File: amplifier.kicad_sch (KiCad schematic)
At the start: 16 parts, among them U5 PAM8403D

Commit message: Added more connections
Updated footprints for pin heads and speakers
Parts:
- removed C13: 470u, Capacitor_SMD:CP_Elec_8x10.5, symbol Device:C
- added C13: 470u, Capacitor_SMD:CP_Elec_8x10.5, symbol Device:C_Polarized
- LS1, LS2: footprint (none) -> Connector_PinHeader_2.00mm:PinHeader_1x02_P2.00mm_Vertical_SMD_Pin1Left
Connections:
- net 3.3V_IN: now also C13.1
- net GND: now also C13.2
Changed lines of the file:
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@@
 	(symbol
 		(lib_id "Device:C")
+		(at 95.25 63.5 0)
+		(unit 1)
+		(exclude_from_sim no)
+		(in_bom yes)
+		(on_board yes)
+		(dnp no)
+		(property "Reference" "C14"
+			(at 88.9 61.976 0)
+			(effects
+				(font
+					(size 1.27 1.27)
+				)
+				(justify left)
+			)
+		)
+		(property "Value" "1u"
+			(at 88.9 64.516 0)
+			(effects
+				(font
+					(size 1.27 1.27)
+				)
+				(justify left)
+			)
+		)
+		(property "Footprint" "Capacitor_SMD:C_0603_1608Metric"
+			(at 96.2152 67.31 0)
+			(effects
+				(font
+					(size 1.27 1.27)
+				)
+				(hide yes)
+			)
+		)
+		(property "Datasheet" "~"
+			(at 95.25 63.5 0)
+			(effects
+				(font
+					(size 1.27 1.27)
+				)
+				(hide yes)
+			)
+		)
+		(property "Description" "Unpolarized capacitor"
+			(at 95.25 63.5 0)
+			(effects
+				(font
+					(size 1.27 1.27)
+				)
+				(hide yes)
+			)
+		)
+		(pin "1"
+		)
+		(pin "2"
+		)
+		(instances
+			(project "plant caretaker"
+				(path "/23b35dcc-615e-4aec-abee-c26cc3d8b906/64bd70cc-1431-45fc-8946-041e9631b1bb"
+					(reference "C14")
+					(unit 1)
+				)
+			)
+		)
+	)
+	(symbol
+		(lib_id "power:GND")
+		(at 165.1 69.85 0)
+		(unit 1)
+		(exclude_from_sim no)
+		(in_bom yes)
+		(on_board yes)
+		(dnp no)
+		(fields_autoplaced yes)
+		(property "Reference" "#PWR033"
+			(at 165.1 76.2 0)
+			(effects
+				(font
+					(size 1.27 1.27)
+				)
+				(hide yes)
+			)
+		)
+		(property "Value" "GND"
+			(at 165.1 74.93 0)
+			(effects
+				(font
+					(size 1.27 1.27)
+				)
+			)
+		)
+		(property "Footprint" ""
+			(at 165.1 69.85 0)
+			(effects
+				(font
+					(size 1.27 1.27)
+				)
+				(hide yes)
+			)
+		)
+		(property "Datasheet" ""
+			(at 165.1 69.85 0)
+			(effects
+				(font
+					(size 1.27 1.27)
+				)
+				(hide yes)
+			)
+		)
+		(property "Description" "Power symbol creates a global label with name \"GND\" , ground"
+			(at 165.1 69.85 0)
+			(effects
+				(font
+					(size 1.27 1.27)
+				)
+				(hide yes)
+			)
+		)
+		(pin "1"
+		)
+		(instances
+			(project "plant caretaker"
+				(path "/23b35dcc-615e-4aec-abee-c26cc3d8b906/64bd70cc-1431-45fc-8946-041e9631b1bb"
+					(reference "#PWR033")
+					(unit 1)
+				)
+			)
+		)
+	)
+	(symbol
+		(lib_id "power:GND")
+		(at 134.62 107.95 0)
+		(unit 1)
+		(exclude_from_sim no)
+		(in_bom yes)
+		(on_board yes)
+		(dnp no)
+		(fields_autoplaced yes)
+		(property "Reference" "#PWR011"
+			(at 134.62 114.3 0)
+			(effects
+				(font
+					(size 1.27 1.27)
+				)
+				(hide yes)
+			)
+		)
+		(property "Value" "GND"
+			(at 134.62 113.03 0)
+			(effects
+				(font
+					(size 1.27 1.27)
+				)
+			)
+		)
+		(property "Footprint" ""
+			(at 134.62 107.95 0)
+			(effects
+				(font
+					(size 1.27 1.27)
+				)
+				(hide yes)
+			)
+		)
+		(property "Datasheet" ""
+			(at 134.62 107.95 0)
+			(effects
+				(font
+					(size 1.27 1.27)
+				)
+				(hide yes)
+			)
+		)
+		(property "Description" "Power symbol creates a global label with name \"GND\" , ground"
+			(at 134.62 107.95 0)
+			(effects
+				(font
+					(size 1.27 1.27)
+				)
+				(hide yes)
+			)
+		)
+		(pin "1"
+		)
+		(instances
+			(project "plant caretaker"
+				(path "/23b35dcc-615e-4aec-abee-c26cc3d8b906/64bd70cc-1431-45fc-8946-041e9631b1bb"
+					(reference "#PWR011")
+					(unit 1)
+				)
+			)
+		)
+	)
+	(symbol
+		(lib_id "Device:C_Polarized")
 		(at 146.05 62.23 0)
 		(unit 1)
@@
 		(fields_autoplaced yes)
 		(property "Reference" "C13"
-			(at 149.86 60.9599 0)
+			(at 149.86 60.0709 0)
 			(effects
 				(font
@@
 		)
 		(property "Value" "470u"
-			(at 149.86 63.4999 0)
+			(at 149.86 62.6109 0)
 			(effects
 				(font
@@
 			)
 		)
-		(property "Description" "Unpolarized capacitor"
+		(property "Description" "Polarized capacitor"
 			(at 146.05 62.23 0)
 			(effects
@@
 			)
 		)
+		(pin "1"
+		)
 		(pin "2"
 		)
-		(pin "1"
-		)
 		(instances
 			(project "plant caretaker"
 				(path "/23b35dcc-615e-4aec-abee-c26cc3d8b906/64bd70cc-1431-45fc-8946-041e9631b1bb"
 					(reference "C13")
-					(unit 1)
-				)
-			)
-		)
-	)
-	(symbol
-		(lib_id "Device:C")
-		(at 95.25 63.5 0)
-		(unit 1)
-		(exclude_from_sim no)
-		(in_bom yes)
-		(on_board yes)
-		(dnp no)
-		(property "Reference" "C14"
-			(at 88.9 61.976 0)
-			(effects
-				(font
-					(size 1.27 1.27)
-				)
-				(justify left)
-			)
-		)
-		(property "Value" "1u"
-			(at 88.9 64.516 0)
-			(effects
-				(font
-					(size 1.27 1.27)
-				)
-				(justify left)
-			)
-		)
-		(property "Footprint" "Capacitor_SMD:C_0603_1608Metric"
-			(at 96.2152 67.31 0)
-			(effects
-				(font
-					(size 1.27 1.27)
-				)
-				(hide yes)
-			)
-		)
-		(property "Datasheet" "~"
-			(at 95.25 63.5 0)
-			(effects
-				(font
-					(size 1.27 1.27)
-				)
-				(hide yes)
-			)
-		)
-		(property "Description" "Unpolarized capacitor"
-			(at 95.25 63.5 0)
-			(effects
-				(font
-					(size 1.27 1.27)
-				)
-				(hide yes)
-			)
-		)
-		(pin "1"
-		)
-		(pin "2"
-		)
-		(instances
-			(project "plant caretaker"
-				(path "/23b35dcc-615e-4aec-abee-c26cc3d8b906/64bd70cc-1431-45fc-8946-041e9631b1bb"
-					(reference "C14")
-					(unit 1)
-				)
-			)
-		)
-	)
-	(symbol
-		(lib_id "power:GND")
-		(at 165.1 69.85 0)
-		(unit 1)
-		(exclude_from_sim no)
-		(in_bom yes)
-		(on_board yes)
-		(dnp no)
-		(fields_autoplaced yes)
-		(property "Reference" "#PWR033"
-			(at 165.1 76.2 0)
-			(effects
-				(font
-					(size 1.27 1.27)
-				)
-				(hide yes)
-			)
-		)
-		(property "Value" "GND"
-			(at 165.1 74.93 0)
-			(effects
-				(font
-					(size 1.27 1.27)
-				)
-			)
-		)
-		(property "Footprint" ""
-			(at 165.1 69.85 0)
-			(effects
-				(font
-					(size 1.27 1.27)
-				)
-				(hide yes)
-			)
-		)
-		(property "Datasheet" ""
-			(at 165.1 69.85 0)
-			(effects
-				(font
-					(size 1.27 1.27)
-				)
-				(hide yes)
-			)
-		)
-		(property "Description" "Power symbol creates a global label with name \"GND\" , ground"
-			(at 165.1 69.85 0)
-			(effects
-				(font
-					(size 1.27 1.27)
-				)
-				(hide yes)
-			)
-		)
-		(pin "1"
-		)
-		(instances
-			(project "plant caretaker"
-				(path "/23b35dcc-615e-4aec-abee-c26cc3d8b906/64bd70cc-1431-45fc-8946-041e9631b1bb"
-					(reference "#PWR033")
-					(unit 1)
-				)
-			)
-		)
-	)
-	(symbol
-		(lib_id "power:GND")
-		(at 134.62 107.95 0)
-		(unit 1)
-		(exclude_from_sim no)
-		(in_bom yes)
-		(on_board yes)
-		(dnp no)
-		(fields_autoplaced yes)
-		(property "Reference" "#PWR011"
-			(at 134.62 114.3 0)
-			(effects
-				(font
-					(size 1.27 1.27)
-				)
-				(hide yes)
-			)
-		)
-		(property "Value" "GND"
-			(at 134.62 113.03 0)
-			(effects
-				(font
-					(size 1.27 1.27)
-				)
-			)
-		)
-		(property "Footprint" ""
-			(at 134.62 107.95 0)
-			(effects
-				(font
-					(size 1.27 1.27)
-				)
-				(hide yes)
-			)
-		)
-		(property "Datasheet" ""
-			(at 134.62 107.95 0)
-			(effects
-				(font
-					(size 1.27 1.27)
-				)
-				(hide yes)
-			)
-		)
-		(property "Description" "Power symbol creates a global label with name \"GND\" , ground"
-			(at 134.62 107.95 0)
-			(effects
-				(font
-					(size 1.27 1.27)
-				)
-				(hide yes)
-			)
-		)
-		(pin "1"
-		)
-		(instances
-			(project "plant caretaker"
-				(path "/23b35dcc-615e-4aec-abee-c26cc3d8b906/64bd70cc-1431-45fc-8946-041e9631b1bb"
-					(reference "#PWR011")
 					(unit 1)
 				)
@@
 			)
 		)
-		(property "Footprint" ""
+		(property "Footprint" "Connector_PinHeader_2.00mm:PinHeader_1x02_P2.00mm_Vertical_SMD_Pin1Left"
 			(at 189.23 110.49 0)
 			(effects
@@
 			)
 		)
-		(property "Footprint" ""
+		(property "Footprint" "Connector_PinHeader_2.00mm:PinHeader_1x02_P2.00mm_Vertical_SMD_Pin1Left"
 			(at 189.23 90.17 0)
 			(effects

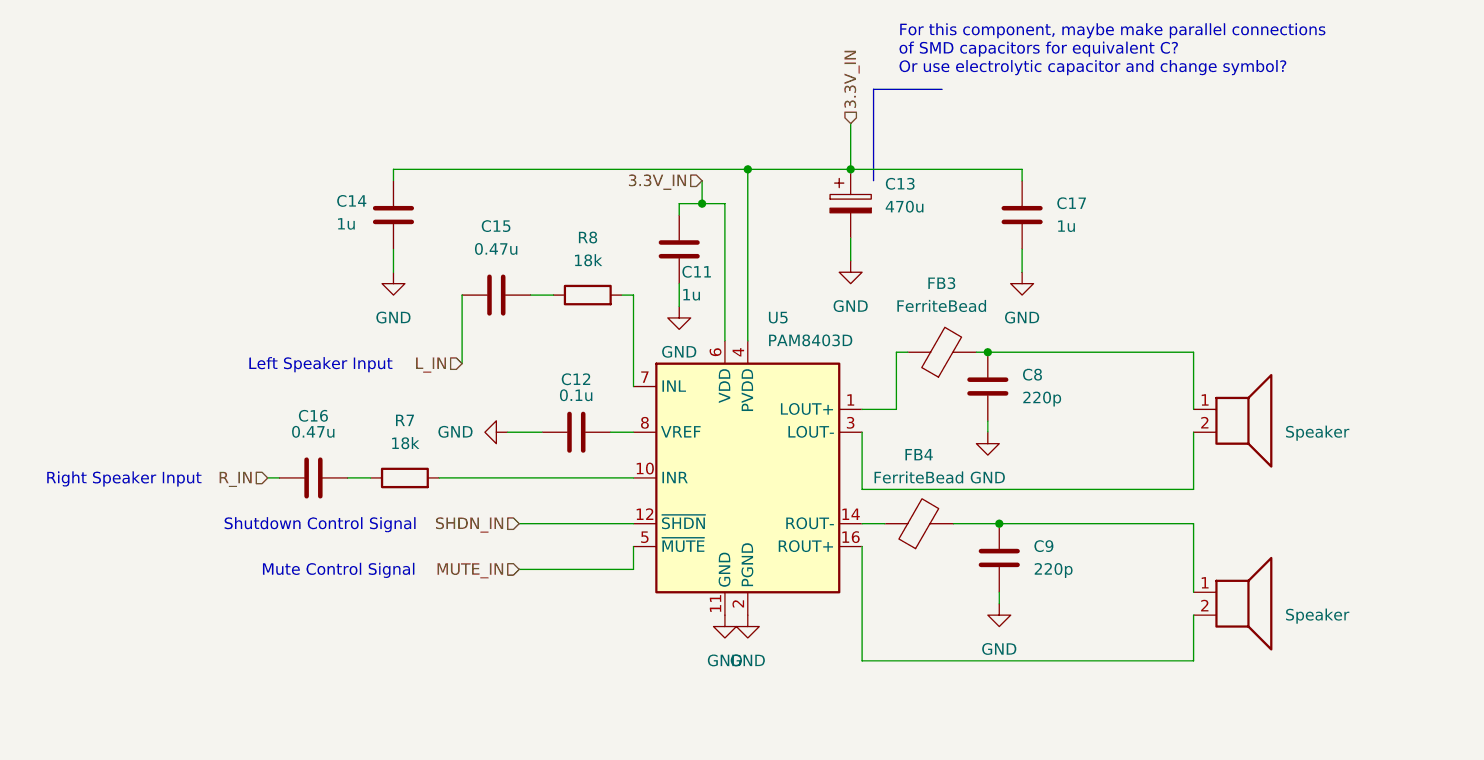
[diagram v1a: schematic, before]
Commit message: Finished PCB
Also added GNDA and GNDD references, to be changed back to GND later. Also added wires connecting ground polygons
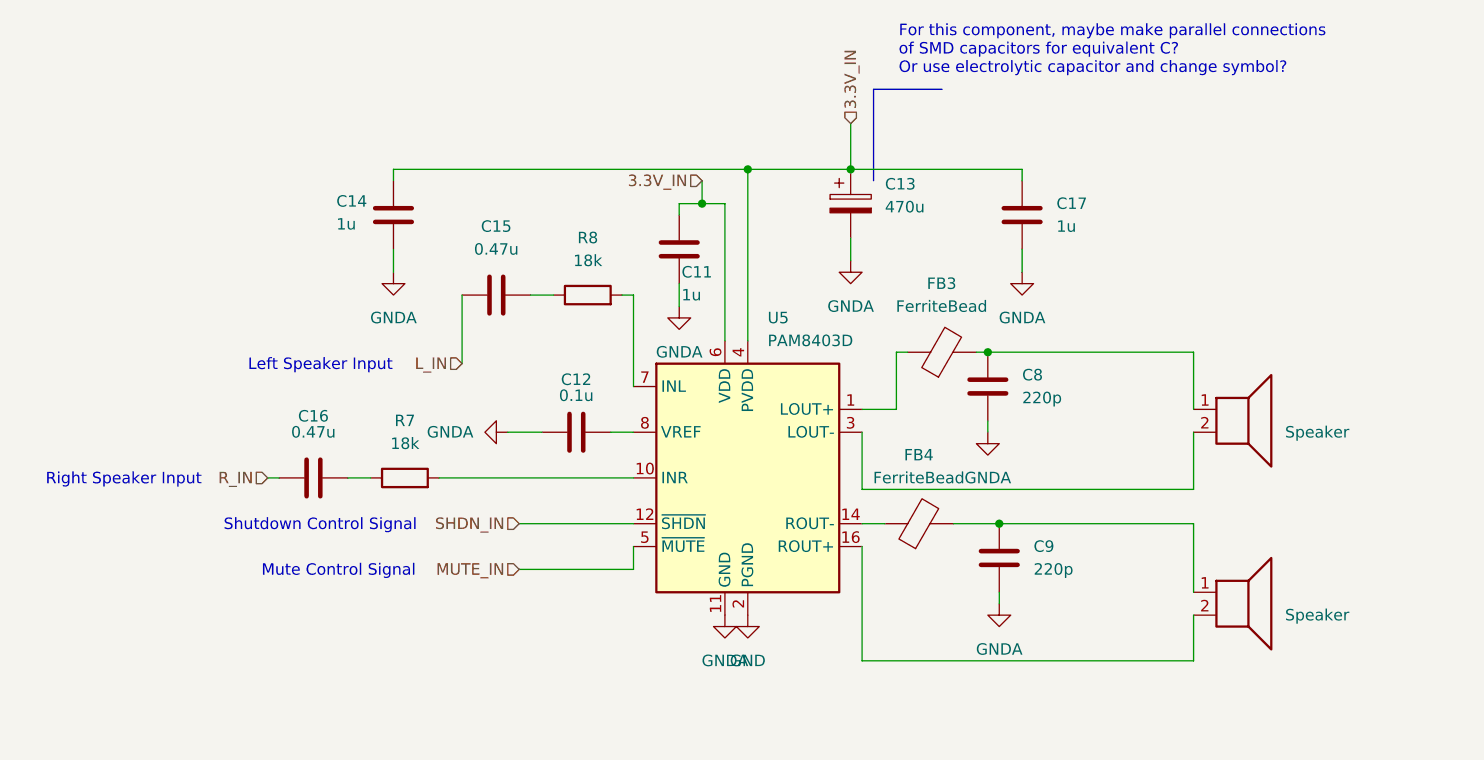
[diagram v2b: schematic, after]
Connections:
- net GND: no longer C11.2, C12.1, C13.2, C14.2, C17.2, C8.2, C9.2, U5.11 (GND)
- new net GNDA: C11.2, C12.1, C13.2, C14.2, C17.2, C8.2, C9.2, U5.11 (GND)
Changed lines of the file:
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@@
 	)
 	(symbol
-		(lib_id "power:GND")
+		(lib_id "power:GNDA")
 		(at 162.56 106.68 0)
 		(unit 1)
@@
 			)
 		)
-		(property "Value" "GND"
+		(property "Value" "GNDA"
 			(at 162.56 111.76 0)
 			(effects
@@
 			)
 		)
-		(property "Description" "Power symbol creates a global label with name \"GND\" , ground"
+		(property "Description" "Power symbol creates a global label with name \"GNDA\" , analog ground"
 			(at 162.56 106.68 0)
 			(effects
@@
 	)
 	(symbol
-		(lib_id "power:GND")
+		(lib_id "power:GNDA")
 		(at 165.1 69.85 0)
 		(unit 1)
@@
 			)
 		)
-		(property "Value" "GND"
+		(property "Value" "GNDA"
 			(at 165.1 74.93 0)
 			(effects
@@
 			)
 		)
-		(property "Description" "Power symbol creates a global label with name \"GND\" , ground"
+		(property "Description" "Power symbol creates a global label with name \"GNDA\" , analog ground"
 			(at 165.1 69.85 0)
 			(effects
@@
 	)
 	(symbol
-		(lib_id "power:GND")
+		(lib_id "power:GNDA")
 		(at 161.29 87.63 0)
 		(unit 1)
@@
 			)
 		)
-		(property "Value" "GND"
+		(property "Value" "GNDA"
 			(at 161.29 92.71 0)
 			(effects
@@
 			)
 		)
-		(property "Description" "Power symbol creates a global label with name \"GND\" , ground"
+		(property "Description" "Power symbol creates a global label with name \"GNDA\" , analog ground"
 			(at 161.29 87.63 0)
 			(effects
@@
 	)
 	(symbol
-		(lib_id "power:GND")
+		(lib_id "power:GNDA")
 		(at 95.25 69.85 0)
 		(unit 1)
@@
 			)
 		)
-		(property "Value" "GND"
+		(property "Value" "GNDA"
 			(at 95.25 74.93 0)
 			(effects
@@
 			)
 		)
-		(property "Description" "Power symbol creates a global label with name \"GND\" , ground"
+		(property "Description" "Power symbol creates a global label with name \"GNDA\" , analog ground"
 			(at 95.25 69.85 0)
 			(effects
@@
 	)
 	(symbol
-		(lib_id "power:GND")
+		(lib_id "power:GNDA")
 		(at 107.95 87.63 270)
 		(unit 1)
@@
 			)
 		)
-		(property "Value" "GND"
+		(property "Value" "GNDA"
 			(at 104.14 87.6299 90)
 			(effects
@@
 			)
 		)
-		(property "Description" "Power symbol creates a global label with name \"GND\" , ground"
+		(property "Description" "Power symbol creates a global label with name \"GNDA\" , analog ground"
 			(at 107.95 87.63 0)
 			(effects
@@
 	)
 	(symbol
-		(lib_id "power:GND")
+		(lib_id "power:GNDA")
 		(at 127 73.66 0)
 		(unit 1)
@@
 			)
 		)
-		(property "Value" "GND"
+		(property "Value" "GNDA"
 			(at 127 78.74 0)
 			(effects
@@
 			)
 		)
-		(property "Description" "Power symbol creates a global label with name \"GND\" , ground"
+		(property "Description" "Power symbol creates a global label with name \"GNDA\" , analog ground"
 			(at 127 73.66 0)
 			(effects
@@
 	)
 	(symbol
-		(lib_id "power:GND")
+		(lib_id "power:GNDA")
 		(at 132.08 107.95 0)
 		(unit 1)
@@
 			)
 		)
-		(property "Value" "GND"
+		(property "Value" "GNDA"
 			(at 132.08 113.03 0)
 			(effects
@@
 			)
 		)
-		(property "Description" "Power symbol creates a global label with name \"GND\" , ground"
+		(property "Description" "Power symbol creates a global label with name \"GNDA\" , analog ground"
 			(at 132.08 107.95 0)
 			(effects
@@
 	)
 	(symbol
-		(lib_id "power:GND")
+		(lib_id "power:GNDA")
 		(at 146.05 68.58 0)
 		(unit 1)
@@
 			)
 		)
-		(property "Value" "GND"
+		(property "Value" "GNDA"
 			(at 146.05 73.66 0)
 			(effects
@@
 			)
 		)
-		(property "Description" "Power symbol creates a global label with name \"GND\" , ground"
+		(property "Description" "Power symbol creates a global label with name \"GNDA\" , analog ground"
 			(at 146.05 68.58 0)
 			(effects

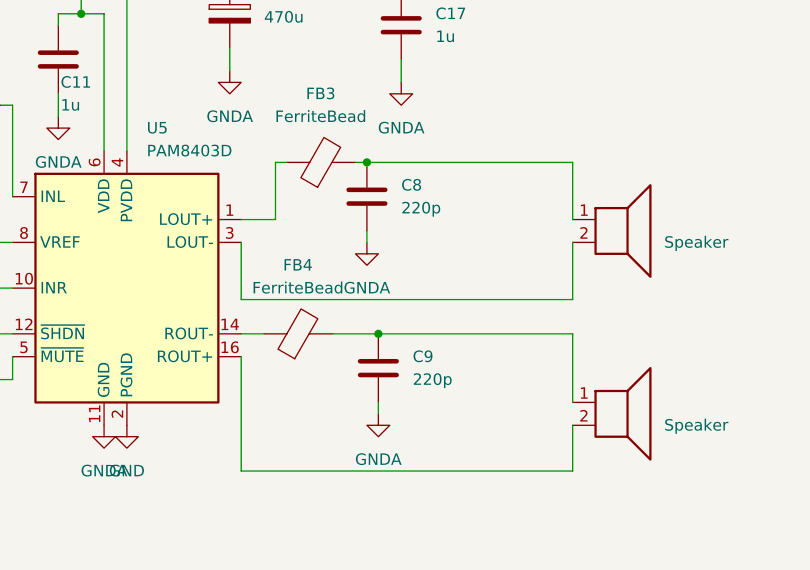
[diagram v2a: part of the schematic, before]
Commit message: Made it smaller
Suddenly I had 81 errors??? Now down to 30 from the codec footprint setup
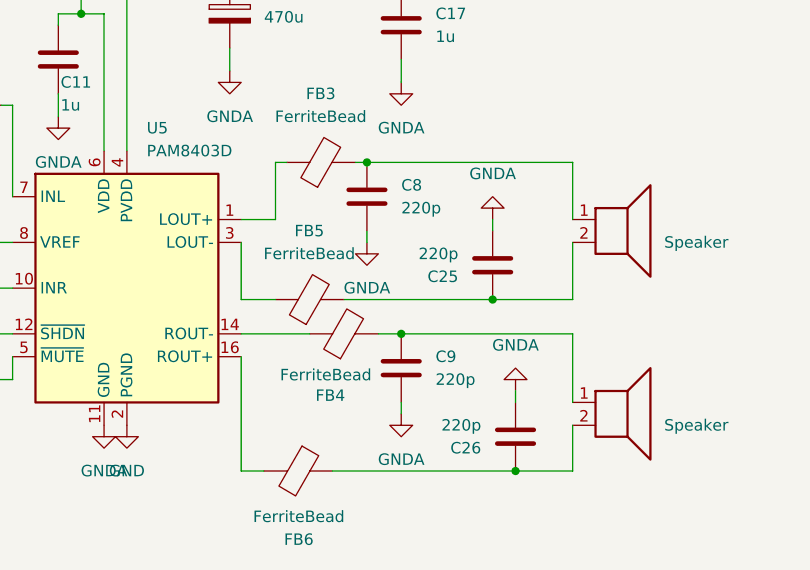
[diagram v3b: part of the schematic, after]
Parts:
- added C25, C26: 220p, Capacitor_SMD:C_0603_1608Metric, symbol Device:C
- added FB5, FB6: FerriteBead, FerriteBead:FerriteBead_742861160_0603, symbol Device:FerriteBead
- FB3, FB4: footprint OtherComponents:FerriteBead_742861160_0603 -> FerriteBead:FerriteBead_742861160_0603
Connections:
- net GNDA: now also C25.2, C26.2
- net at LS2.2: now also C26.1, FB6.1; no longer U5.16 (ROUT+)
- net at LS1.2: now also C25.1, FB5.2; no longer U5.3 (LOUT-)
- new net: FB6.2, U5.16 (ROUT+)
- new net: FB5.1, U5.3 (LOUT-)
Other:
- moved on the sheet: C9, FB4
